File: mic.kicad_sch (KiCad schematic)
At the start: 7 parts, among them U3 ADAU7002ACBZ-R7

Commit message: added test points
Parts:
- added TP5: TestPoint PDM DAT, TestPoint:TestPoint_Pad_D1.5mm, symbol Connector:TestPoint
- added TP6: TestPoint PDM CLK, TestPoint:TestPoint_Pad_D1.5mm, symbol Connector:TestPoint
- added TP7: TestPoint_LRCLK, TestPoint:TestPoint_Pad_D1.5mm, symbol Connector:TestPoint
- added TP8: TestPoint_BCLK, TestPoint:TestPoint_Pad_D1.5mm, symbol Connector:TestPoint
- added TP9: TestPoint_DIN, TestPoint:TestPoint_Pad_D1.5mm, symbol Connector:TestPoint
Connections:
- net BCLK: now also TP8.1
- net DIN: now also TP9.1
- net FSYNC_LRCLK: now also TP7.1
- net PDM_CLK: now also TP6.1
- net PDM_DAT: now also TP5.1
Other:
- note added: "Could get rid of this?"
- note removed: "MAKE SMALLER"

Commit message: poured ground layer added RF keep out
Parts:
- TP5, TP6, TP7, TP8, TP9: footprint TestPoint:TestPoint_Pad_D1.5mm -> TestPoint:TestPoint_Pad_D1.0mm
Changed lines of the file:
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@@
 			)
 		)
-		(property "Footprint" "TestPoint:TestPoint_Pad_D1.5mm"
+		(property "Footprint" "TestPoint:TestPoint_Pad_D1.0mm"
 			(at 133.35 88.9 0)
 			(effects
@@
 			)
 		)
-		(property "Footprint" "TestPoint:TestPoint_Pad_D1.5mm"
+		(property "Footprint" "TestPoint:TestPoint_Pad_D1.0mm"
 			(at 189.23 93.98 0)
 			(effects
@@
 			)
 		)
-		(property "Footprint" "TestPoint:TestPoint_Pad_D1.5mm"
+		(property "Footprint" "TestPoint:TestPoint_Pad_D1.0mm"
 			(at 142.24 86.36 0)
 			(effects
@@
 			)
 		)
-		(property "Footprint" "TestPoint:TestPoint_Pad_D1.5mm"
+		(property "Footprint" "TestPoint:TestPoint_Pad_D1.0mm"
 			(at 156.21 110.49 0)
 			(effects
@@
 			)
 		)
-		(property "Footprint" "TestPoint:TestPoint_Pad_D1.5mm"
+		(property "Footprint" "TestPoint:TestPoint_Pad_D1.0mm"
 			(at 146.05 93.98 0)
 			(effects

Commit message: routed audio
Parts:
- removed TP5: TestPoint PDM DAT, TestPoint:TestPoint_Pad_D1.0mm, symbol Connector:TestPoint
- removed TP6: TestPoint PDM CLK, TestPoint:TestPoint_Pad_D1.0mm, symbol Connector:TestPoint
- added J5: J_000003, mic_patch_parts:J_00003, symbol mic_patch_parts:J_00003
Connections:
- net PDM_CLK: now also J5.1
- net PDM_DAT: now also J5.2
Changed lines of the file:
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@@
-	)
-	(junction
-		(at 138.43 88.9)
-		(diameter 0)
-		(color 0 0 0 0)
 	)
 	(junction
@@
 	)
 	(junction
+		(at 148.59 90.17)
+		(diameter 0)
+		(color 0 0 0 0)
+	)
+	(junction
 		(at 109.22 81.28)
 		(diameter 0)
@@
 	)
 	(junction
+		(at 151.13 86.36)
+		(diameter 0)
+		(color 0 0 0 0)
+	)
+	(junction
 		(at 80.01 81.28)
 		(diameter 0)
@@
 		(color 0 0 0 0)
 	)
-	(junction
-		(at 137.16 86.36)
-		(diameter 0)
-		(color 0 0 0 0)
-	)
 	(wire
 		(pts
@@
 	(wire
 		(pts
+			(xy 151.13 86.36) (xy 157.48 86.36)
+		)
+		(stroke
+			(width 0)
+			(type default)
+		)
+	)
+	(wire
+		(pts
 			(xy 119.38 91.44) (xy 123.19 91.44)
 		)
@@
 	(wire
 		(pts
-			(xy 138.43 88.9) (xy 142.24 88.9)
-		)
-		(stroke
-			(width 0)
-			(type default)
-		)
-	)
-	(wire
-		(pts
 			(xy 109.22 96.52) (xy 109.22 99.06)
 		)
@@
 	(wire
 		(pts
+			(xy 151.13 71.12) (xy 151.13 86.36)
+		)
+		(stroke
+			(width 0)
+			(type default)
+		)
+	)
+	(wire
+		(pts
 			(xy 161.29 110.49) (xy 153.67 110.49)
 		)
@@
 	(wire
 		(pts
-			(xy 128.27 86.36) (xy 137.16 86.36)
-		)
-		(stroke
-			(width 0)
-			(type default)
-		)
-	)
-	(wire
-		(pts
 			(xy 185.42 93.98) (xy 194.31 93.98)
 		)
@@
 	(wire
 		(pts
-			(xy 142.24 90.17) (xy 157.48 90.17)
+			(xy 142.24 90.17) (xy 148.59 90.17)
 		)
 		(stroke
@@
 	(wire
 		(pts
+			(xy 148.59 68.58) (xy 151.13 68.58)
+		)
+		(stroke
+			(width 0)
+			(type default)
+		)
+	)
+	(wire
+		(pts
 			(xy 185.42 86.36) (xy 212.09 86.36)
 		)
@@
 	(wire
 		(pts
-			(xy 119.38 88.9) (xy 138.43 88.9)
-		)
-		(stroke
-			(width 0)
-			(type default)
-		)
-	)
-	(wire
-		(pts
-			(xy 137.16 86.36) (xy 157.48 86.36)
+			(xy 119.38 88.9) (xy 142.24 88.9)
+		)
+		(stroke
+			(width 0)
+			(type default)
+		)
+	)
+	(wire
+		(pts
+			(xy 128.27 86.36) (xy 151.13 86.36)
 		)
 		(stroke
@@
 	(wire
 		(pts
+			(xy 148.59 68.58) (xy 148.59 90.17)
+		)
+		(stroke
+			(width 0)
+			(type default)
+		)
+	)
+	(wire
+		(pts
 			(xy 148.59 93.98) (xy 151.13 93.98)
 		)
@@
 		(pts
 			(xy 80.01 81.28) (xy 109.22 81.28)
+		)
+		(stroke
+			(width 0)
+			(type default)
+		)
+	)
+	(wire
+		(pts
+			(xy 148.59 90.17) (xy 157.48 90.17)
 		)
 		(stroke
@@
 	)
 	(symbol
-		(lib_id "Connector:TestPoint")
-		(at 138.43 88.9 180)
+		(lib_id "mic_patch_parts:J_00003")
+		(at 152.4 73.66 0)
 		(unit 1)
 		(exclude_from_sim no)
@@
 		(on_board yes)
 		(dnp no)
-		(property "Reference" "TP6"
-			(at 140.208 93.98 0)
+		(fields_autoplaced yes)
+		(property "Reference" "J5"
+			(at 157.48 67.3099 0)
 			(effects
 				(font
@@
 			)
 		)
-		(property "Value" "TestPoint PDM CLK"
-			(at 135.128 91.948 90)
+		(property "Value" "J_000003"
+			(at 157.48 69.8499 0)
 			(effects
 				(font
@@
 			)
 		)
-		(property "Footprint" "TestPoint:TestPoint_Pad_D1.0mm"
-			(at 133.35 88.9 0)
-			(effects
-				(font
-					(size 1.27 1.27)
-				)
-				(hide yes)
-			)
-		)
-		(property "Datasheet" "~"
-			(at 133.35 88.9 0)
-			(effects
-				(font
-					(size 1.27 1.27)
-				)
-				(hide yes)
-			)
-		)
-		(property "Description" "test point"
-			(at 138.43 88.9 0)
+		(property "Footprint" "mic_patch_parts:J_00003"
+			(at 159.004 81.788 0)
+			(effects
+				(font
+					(size 1.27 1.27)
+				)
+				(hide yes)
+			)
+		)
+		(property "Datasheet" ""
+			(at 153.67 71.12 0)
+			(effects
+				(font
+					(size 1.27 1.27)
+				)
+				(hide yes)
+			)
+		)
+		(property "Description" "JST SH 2 Pin Straight Connector"
+			(at 155.194 62.484 0)
+			(effects
+				(font
+					(size 1.27 1.27)
+				)
+				(hide yes)
+			)
+		)
+		(property "Desc" "JST SH"
+			(at 157.48 72.3899 0)
+			(effects
+				(font
+					(size 1.27 1.27)
+				)
+				(justify left)
+			)
+		)
+		(property "LCSC PNs" "C7430451"
+			(at 153.924 75.438 0)
 			(effects
 				(font
@@
 		)
 		(pin "1"
+		)
+		(pin "2"
 		)
 		(instances
 			(project "mic_patch_v1"
 				(path "/5448a297-4261-40a5-8009-47199bfe22cb/134a282e-9ca3-4100-8ce3-f798951ef007"
-					(reference "TP6")
+					(reference "J5")
 					(unit 1)
 				)
@@
 					(unit 1)
 				)
-			)
-		)
-	)
-	(symbol
-		(lib_id "Connector:TestPoint")
-		(at 137.16 86.36 0)
-		(unit 1)
-		(exclude_from_sim no)
-		(in_bom yes)
-		(on_board yes)
-		(dnp no)
-		(property "Reference" "TP5"
-			(at 135.382 81.28 0)
-			(effects
-				(font
-					(size 1.27 1.27)
-				)
-				(justify left)
-			)
-		)
-		(property "Value" "TestPoint PDM DAT"
-			(at 131.826 78.486 0)
-			(effects
-				(font
-					(size 1.27 1.27)
-				)
-				(justify left)
-			)
-		)
-		(property "Footprint" "TestPoint:TestPoint_Pad_D1.0mm"
-			(at 142.24 86.36 0)
-			(effects
-				(font
-					(size 1.27 1.27)
-				)
-				(hide yes)
-			)
-		)
-		(property "Datasheet" "~"
-			(at 142.24 86.36 0)
-			(effects
-				(font
-					(size 1.27 1.27)
-				)
-				(hide yes)
-			)
-		)
-		(property "Description" "test point"
-			(at 137.16 86.36 0)
-			(effects
-				(font
-					(size 1.27 1.27)
-				)
-				(hide yes)
-			)
-		)
-		(pin "1"
-		)
-		(instances
-			(project "mic_patch_v1"
-				(path "/5448a297-4261-40a5-8009-47199bfe22cb/134a282e-9ca3-4100-8ce3-f798951ef007"
-					(reference "TP5")
-					(unit 1)
-				)

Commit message: removed PDM series termination resistor under guidance from MS-2472 analogue devices
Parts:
- removed R6: R_00005, Resistor_SMD:R_0402_1005Metric, symbol mic_patch_parts:R_00005
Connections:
- net PDM_DAT: now also MK1.1 (DATA)
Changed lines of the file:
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@@
-	(wire
-		(pts
-			(xy 128.27 86.36) (xy 151.13 86.36)
-		)
-		(stroke
-			(width 0)
-			(type default)
-		)
-	)
 	(wire
 		(pts
@@
 	(wire
 		(pts
-			(xy 119.38 86.36) (xy 123.19 86.36)
+			(xy 119.38 86.36) (xy 151.13 86.36)
 		)
 		(stroke
@@
 					(unit 1)
 				)
-			)
-		)
-	)
-	(symbol
-		(lib_id "mic_patch_parts:R_00005")
-		(at 125.73 86.36 90)
-		(unit 1)
-		(exclude_from_sim no)
-		(in_bom yes)
-		(on_board yes)
-		(dnp no)
-		(fields_autoplaced yes)
-		(property "Reference" "R6"
-			(at 125.73 78.74 90)
-			(effects
-				(font
-					(size 1.27 1.27)
-				)
-			)
-		)
-		(property "Value" "R_00005"
-			(at 125.73 81.28 90)
-			(effects
-				(font
-					(size 1.27 1.27)
-				)
-			)
-		)
-		(property "Footprint" "Resistor_SMD:R_0402_1005Metric"
-			(at 125.73 86.36 0)
-			(effects
-				(font
-					(size 1.27 1.27)
-				)
-				(hide yes)
-			)
-		)
-		(property "Datasheet" "~"
-			(at 125.73 86.36 0)
-			(effects
-				(font
-					(size 1.27 1.27)
-				)
-				(hide yes)
-			)
-		)
-		(property "Description" "100Ω resistor"
-			(at 125.73 86.36 0)
-			(effects
-				(font
-					(size 1.27 1.27)
-				)
-				(hide yes)
-			)
-		)
-		(property "Desc" "100Ω "
-			(at 125.73 83.82 90)
-			(effects
-				(font
-					(size 1.27 1.27)
-				)
-			)
-		)
-		(property "MPNs" "0402WGF1000TCE"
-			(at 125.73 86.36 0)
-			(effects
-				(font
-					(size 1.27 1.27)
-				)
-				(hide yes)
-			)
-		)
-		(property "LCSC PNs" "C25076"
-			(at 125.73 86.36 0)
-			(effects
-				(font
-					(size 1.27 1.27)
-				)
-				(hide yes)
-			)
-		)
-		(pin "2"
-		)
-		(pin "1"
-		)
-		(instances
-			(project "mic_patch_v1"
-				(path "/5448a297-4261-40a5-8009-47199bfe22cb/134a282e-9ca3-4100-8ce3-f798951ef007"
-					(reference "R6")
-					(unit 1)
-				)

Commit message: corrected missing part numbers + inconsistencies
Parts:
- R7: value R_00002 -> R_00003
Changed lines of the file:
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@@
 			)
 		)
-		(property "Value" "R_00002"
+		(property "Value" "R_00003"
 			(at 125.73 96.5199 0)
 			(effects

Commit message: added solder jumper to configure mic
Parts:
- added JP1: SolderJumper_3_Open, Jumper:SolderJumper-3_P1.3mm_Open_Pad1.0x1.5mm_NumberLabels, symbol Jumper:SolderJumper_3_Open
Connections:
- net +3V0 VDD_NRF: now also JP1.1 (A)
- net GND: now also JP1.3 (B); no longer R7.2
- new net: JP1.2 (C), R7.2
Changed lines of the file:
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@@
+	(wire
+		(pts
+			(xy 128.27 105.41) (xy 128.27 111.76)
+		)
+		(stroke
+			(width 0)
+			(type default)
+		)
+	)
 	(wire
 		(pts
@@
 	(wire
 		(pts
+			(xy 123.19 99.06) (xy 123.19 101.6)
+		)
+		(stroke
+			(width 0)
+			(type default)
+		)
+	)
+	(wire
+		(pts
 			(xy 153.67 97.79) (xy 157.48 97.79)
 		)
@@
 	(wire
 		(pts
+			(xy 118.11 105.41) (xy 118.11 110.49)
+		)
+		(stroke
+			(width 0)
+			(type default)
+		)
+	)
+	(wire
+		(pts
 			(xy 123.19 91.44) (xy 123.19 93.98)
 		)
@@
 		(pts
 			(xy 119.38 86.36) (xy 151.13 86.36)
-		)
-		(stroke
-			(width 0)
-			(type default)
-		)
-	)
-	(wire
-		(pts
-			(xy 123.19 99.06) (xy 123.19 100.33)
 		)
 		(stroke
@@
 	(text "DIN: Optional Pull down resistor\n"
 		(exclude_from_sim no)
-		(at 118.11 118.364 0)
+		(at 118.11 126.238 0)
 		(effects
 			(font
@@
 	(symbol
 		(lib_id "power:GND")
-		(at 123.19 100.33 0)
+		(at 118.11 110.49 0)
 		(unit 1)
 		(exclude_from_sim no)
@@
 		(dnp no)
 		(property "Reference" "#PWR042"
-			(at 123.19 106.68 0)
+			(at 118.11 116.84 0)
 			(effects
 				(font
@@
 		)
 		(property "Value" "GND"
-			(at 123.19 104.14 0)
+			(at 118.11 114.3 0)
 			(effects
 				(font
@@
 		)
 		(property "Footprint" ""
-			(at 123.19 100.33 0)
+			(at 118.11 110.49 0)
 			(effects
 				(font
@@
 		)
 		(property "Datasheet" ""
-			(at 123.19 100.33 0)
+			(at 118.11 110.49 0)
 			(effects
 				(font
@@
 		)
 		(property "Description" "Power symbol creates a global label with name \"GND\" , ground"
-			(at 123.19 100.33 0)
+			(at 118.11 110.49 0)
 			(effects
 				(font
@@
 				(path "/5448a297-4261-40a5-8009-47199bfe22cb/134a282e-9ca3-4100-8ce3-f798951ef007"
 					(reference "#PWR042")
+					(unit 1)
+				)
+			)
+		)
+	)
+	(symbol
+		(lib_id "power:+1V8")
+		(at 128.27 111.76 180)
+		(unit 1)
+		(exclude_from_sim no)
+		(in_bom yes)
+		(on_board yes)
+		(dnp no)
+		(property "Reference" "#PWR021"
+			(at 128.27 107.95 0)
+			(effects
+				(font
+					(size 1.27 1.27)
+				)
+				(hide yes)
+			)
+		)
+		(property "Value" "+3V0 VDD_NRF"
+			(at 128.778 116.586 0)
+			(effects
+				(font
+					(size 1.27 1.27)
+				)
+			)
+		)
+		(property "Footprint" ""
+			(at 128.27 111.76 0)
+			(effects
+				(font
+					(size 1.27 1.27)
+				)
+				(hide yes)
+			)
+		)
+		(property "Datasheet" ""
+			(at 128.27 111.76 0)
+			(effects
+				(font
+					(size 1.27 1.27)
+				)
+				(hide yes)
+			)
+		)
+		(property "Description" "Power symbol creates a global label with name \"+1V8\""
+			(at 128.27 111.76 0)
+			(effects
+				(font
+					(size 1.27 1.27)
+				)
+				(hide yes)
+			)
+		)
+		(pin "1"
+		)
+		(instances
+			(project "mic_patch_v1"
+				(path "/5448a297-4261-40a5-8009-47199bfe22cb/134a282e-9ca3-4100-8ce3-f798951ef007"
+					(reference "#PWR021")
 					(unit 1)
 				)
@@
 					(unit 1)
 				)
+			)
+		)
+	)
+	(symbol
+		(lib_id "Jumper:SolderJumper_3_Open")
+		(at 123.19 105.41 180)
+		(unit 1)
+		(exclude_from_sim yes)
+		(in_bom no)
+		(on_board yes)
+		(dnp no)
+		(property "Reference" "JP1"
+			(at 142.24 112.776 0)
+			(effects
+				(font
+					(size 1.27 1.27)
+				)
+			)
+		)
+		(property "Value" "SolderJumper_3_Open"
+			(at 142.24 115.316 0)
+			(effects
+				(font
+					(size 1.27 1.27)
+				)
+			)
+		)
+		(property "Footprint" "Jumper:SolderJumper-3_P1.3mm_Open_Pad1.0x1.5mm_NumberLabels"
+			(at 123.19 105.41 0)
+			(effects
+				(font
+					(size 1.27 1.27)
+				)
+				(hide yes)
+			)
+		)
+		(property "Datasheet" "~"
+			(at 123.19 105.41 0)
+			(effects
+				(font
+					(size 1.27 1.27)
+				)
+				(hide yes)
+			)
+		)
+		(property "Description" "Solder Jumper, 3-pole, open"
+			(at 123.19 105.41 0)
+			(effects
+				(font
+					(size 1.27 1.27)
+				)
+				(hide yes)
+			)
+		)
+		(pin "2"
+		)
+		(pin "3"
+		)
+		(pin "1"
+		)
+		(instances
+			(project "mic_patch_v1"
+				(path "/5448a297-4261-40a5-8009-47199bfe22cb/134a282e-9ca3-4100-8ce3-f798951ef007"
+					(reference "JP1")
+					(unit 1)
+				)

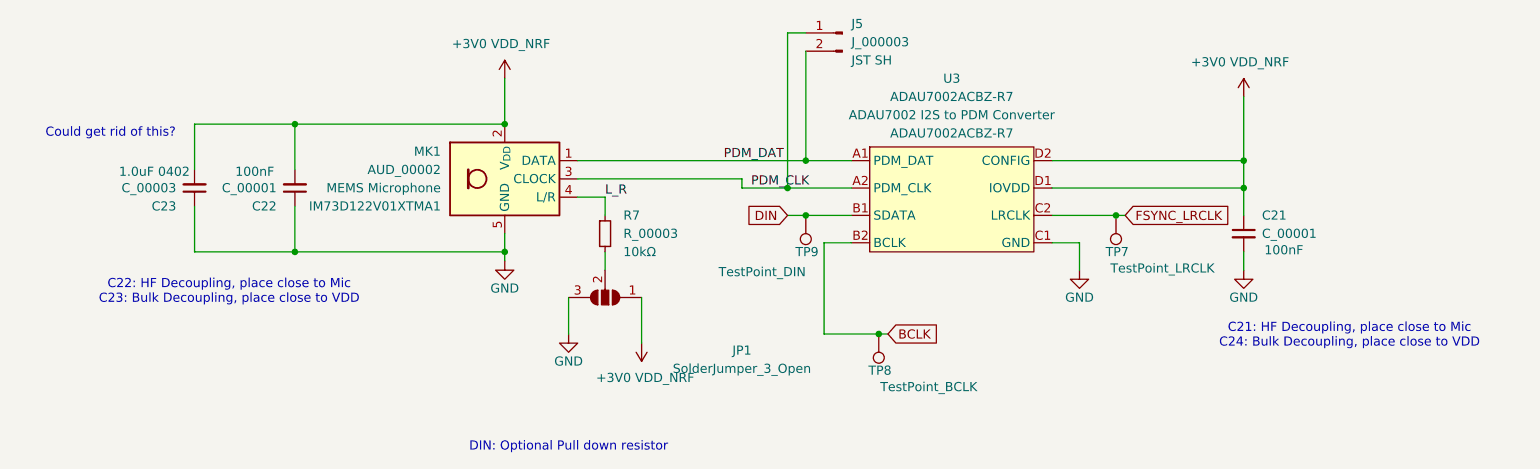
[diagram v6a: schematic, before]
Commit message: Removed ADAU7002, + test points
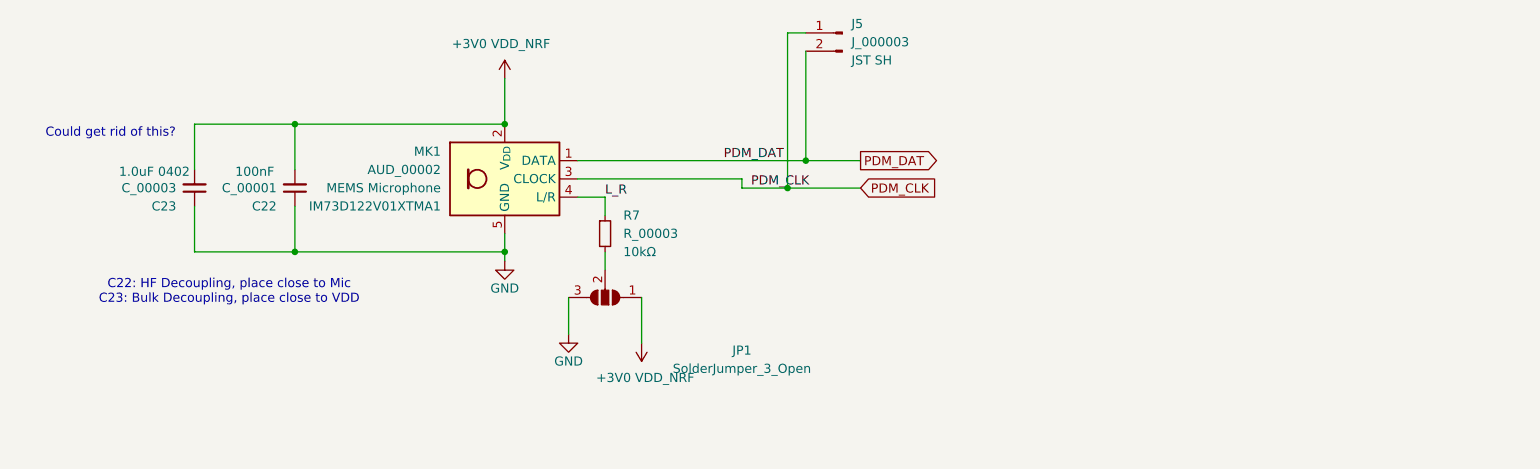
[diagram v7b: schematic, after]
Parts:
- removed C21: C_00001, Capacitor_SMD:C_0402_1005Metric, symbol mic_patch_parts:C_00001
- removed TP7: TestPoint_LRCLK, TestPoint:TestPoint_Pad_D1.0mm, symbol Connector:TestPoint
- removed TP8: TestPoint_BCLK, TestPoint:TestPoint_Pad_D1.0mm, symbol Connector:TestPoint
- removed TP9: TestPoint_DIN, TestPoint:TestPoint_Pad_D1.0mm, symbol Connector:TestPoint
- removed U3: ADAU7002ACBZ-R7, mic_patch_parts:ADAU7002ACBZ-R7, symbol mic_patch_parts:AUD_00001
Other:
- note removed: "C21: HF Decoupling, place close to Mic C24: Bulk Decoupling, place close to VDD"
- note removed: "DIN: Optional Pull down resistor"

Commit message: Removed SD Card from schematic
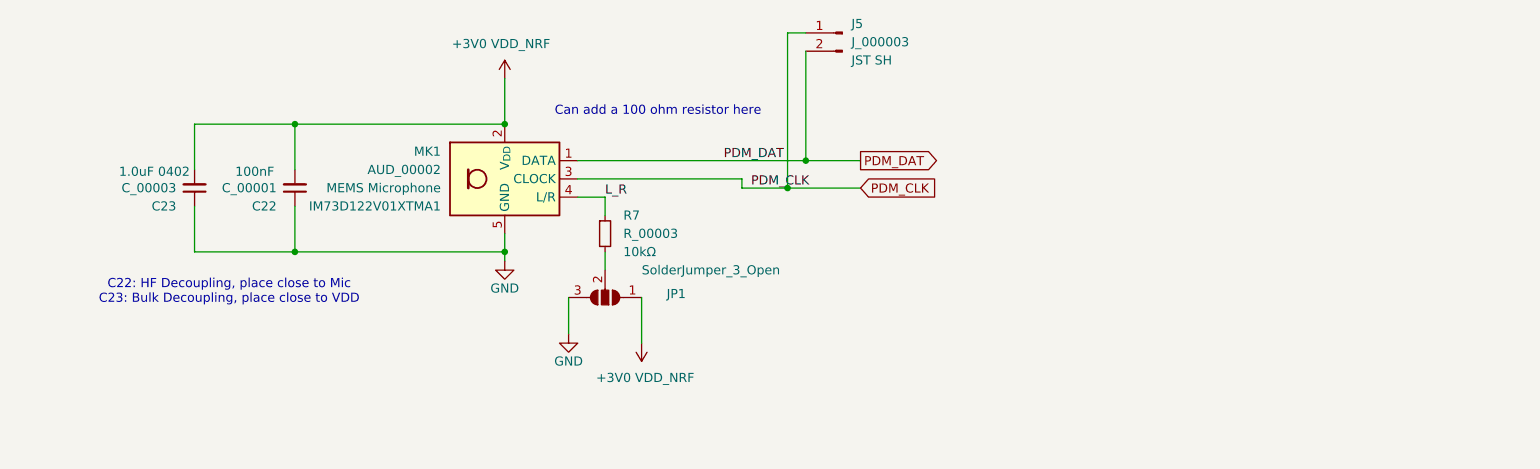
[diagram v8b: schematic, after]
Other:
- note added: "Can add a 100 ohm resistor here"
- note removed: "Could get rid of this?"
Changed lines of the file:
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@@
 		)
 	)
-	(text "Could get rid of this?\n"
-		(exclude_from_sim no)
-		(at 54.356 82.55 0)
+	(text "Can add a 100 ohm resistor here\n"
+		(exclude_from_sim no)
+		(at 130.556 79.502 0)
 		(effects
 			(font
@@
 		(dnp no)
 		(property "Reference" "JP1"
-			(at 142.24 112.776 0)
+			(at 133.096 104.902 0)
 			(effects
 				(font
@@
 		)
 		(property "Value" "SolderJumper_3_Open"
-			(at 142.24 115.316 0)
-			(effects
-				(font
+			(at 137.922 101.6 0)
+			(effects
+				(font
